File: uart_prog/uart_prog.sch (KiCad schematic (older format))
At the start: 22 parts, among them J1 USB_B_Micro, J2 Conn_01x06, Q1 MBT3904DW1, SW1 SW_SPDT, U1 FT231XQ

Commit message: Layout doner
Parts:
- removed TP1, TP2: TestPoint, TestPoint:TestPoint_THTPad_D2.0mm_Drill1.0mm, symbol Connector:TestPoint
- C3: footprint Capacitor_SMD:C_01005_0402Metric -> Capacitor_SMD:C_0805_2012Metric_Pad1.18x1.45mm_HandSolder
- J1: symbol Connector:USB_B_Micro -> uart_prog-rescue:USB_B_Micro-Connector
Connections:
- net BOOT_OPT: now also J2.2 (Pin_2); no longer J2.4 (Pin_4)
- net EN: now also J2.1 (Pin_1); no longer J2.3 (Pin_3)
- net rx: now also J2.3 (Pin_3); no longer J2.1 (Pin_1)
- net tx: now also J2.4 (Pin_4); no longer J2.2 (Pin_2)
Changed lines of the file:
@@
 $EndComp
 $Comp
-L Connector:USB_B_Micro J1
+L uart_prog-rescue:USB_B_Micro-Connector J1
 U 1 1 608888FB
 P 2700 3450
@@
 	1    0    0    -1
 $EndComp
-Text GLabel 8400 3350 0    50   Input ~ 0
+Text GLabel 8400 3550 0    50   Input ~ 0
 rx
-Text GLabel 8400 3450 0    50   Input ~ 0
+Text GLabel 8400 3650 0    50   Input ~ 0
 tx
 Text GLabel 8400 3750 0    50   Input ~ 0
 5v
-Text GLabel 8400 3550 0    50   Input ~ 0
+Text GLabel 8400 3350 0    50   Input ~ 0
 EN
-Text GLabel 8400 3650 0    50   Input ~ 0
+Text GLabel 8400 3450 0    50   Input ~ 0
 BOOT_OPT
 $Comp
@@
 F 0 "C3" H 4392 2596 50  0000 L CNN
 F 1 "22u" H 4392 2505 50  0000 L CNN
-F 2 "Capacitor_SMD:C_01005_0402Metric" H 4300 2550 50  0001 C CNN
+F 2 "Capacitor_SMD:C_0805_2012Metric_Pad1.18x1.45mm_HandSolder" H 4300 2550 50  0001 C CNN
 F 3 "~" H 4300 2550 50  0001 C CNN
 	1    4300 2550
@@
 Text GLabel 8200 2350 3    50   Input ~ 0
 rxled
+Text GLabel 8200 1950 1    50   Input ~ 0
+vccio
+$Comp
+L Device:R_Small R6
+U 1 1 6090552B
+P 8600 2050
+F 0 "R6" V 8404 2050 50  0000 C CNN
+F 1 "270" V 8495 2050 50  0000 C CNN
+F 2 "Resistor_SMD:R_0805_2012Metric_Pad1.15x1.40mm_HandSolder" H 8600 2050 50  0001 C CNN
+F 3 "~" H 8600 2050 50  0001 C CNN
+	1    8600 2050
+	-1   0    0    1
+$EndComp
+Text GLabel 8600 2350 3    50   Input ~ 0
+txled
+Text GLabel 8600 1950 1    50   Input ~ 0
+vccio
+Text Label 3300 3450 0    50   ~ 0
+in+
+Text Label 3250 3550 0    50   ~ 0
+in-
+Text Label 4300 3500 0    50   ~ 0
+in2+
+Text Label 4250 3450 0    50   ~ 0
+in2-
+$Comp
+L Device:LED_Small D2
+U 1 1 60905532
+P 8600 2250
+F 0 "D2" V 8646 2182 50  0000 R CNN
+F 1 "yellow" V 8555 2182 50  0000 R CNN
+F 2 "LED_SMD:LED_0805_2012Metric_Pad1.15x1.40mm_HandSolder" V 8600 2250 50  0001 C CNN
+F 3 "~" V 8600 2250 50  0001 C CNN
+	1    8600 2250
+	0    -1   -1   0
+$EndComp
 $Comp
 L Device:LED_Small D1
@@
 	0    -1   -1   0
 $EndComp
-Text GLabel 8200 1950 1    50   Input ~ 0
-vccio
-$Comp
-L Device:R_Small R6
-U 1 1 6090552B
-P 8600 2050
-F 0 "R6" V 8404 2050 50  0000 C CNN
-F 1 "270" V 8495 2050 50  0000 C CNN
-F 2 "Resistor_SMD:R_0805_2012Metric_Pad1.15x1.40mm_HandSolder" H 8600 2050 50  0001 C CNN
-F 3 "~" H 8600 2050 50  0001 C CNN
-	1    8600 2050
-	-1   0    0    1
-$EndComp
-Text GLabel 8600 2350 3    50   Input ~ 0
-txled
-$Comp
-L Device:LED_Small D2
-U 1 1 60905532
-P 8600 2250
-F 0 "D2" V 8646 2182 50  0000 R CNN
-F 1 "yellow" V 8555 2182 50  0000 R CNN
-F 2 "LED_SMD:LED_0805_2012Metric_Pad1.15x1.40mm_HandSolder" V 8600 2250 50  0001 C CNN
-F 3 "~" V 8600 2250 50  0001 C CNN
-	1    8600 2250
-	0    -1   -1   0
-$EndComp
-Text GLabel 8600 1950 1    50   Input ~ 0
-vccio
-Text GLabel 8400 4350 0    50   Input ~ 0
-dtr
-Text GLabel 8400 4550 0    50   Input ~ 0
-rts
-$Comp
-L Connector:TestPoint TP1
-U 1 1 6090AF77
-P 8400 4350
-F 0 "TP1" V 8354 4538 50  0000 L CNN
-F 1 "TestPoint" V 8445 4538 50  0000 L CNN
-F 2 "TestPoint:TestPoint_THTPad_D2.0mm_Drill1.0mm" H 8600 4350 50  0001 C CNN
-F 3 "~" H 8600 4350 50  0001 C CNN
-	1    8400 4350
-	0    1    1    0
-$EndComp
-$Comp
-L Connector:TestPoint TP2
-U 1 1 6090B50B
-P 8400 4550
-F 0 "TP2" V 8354 4738 50  0000 L CNN
-F 1 "TestPoint" V 8445 4738 50  0000 L CNN
-F 2 "TestPoint:TestPoint_THTPad_D2.0mm_Drill1.0mm" H 8600 4550 50  0001 C CNN
-F 3 "~" H 8600 4550 50  0001 C CNN
-	1    8400 4550
-	0    1    1    0
-$EndComp
-Text Label 3300 3450 0    50   ~ 0
-in+
-Text Label 3250 3550 0    50   ~ 0
-in-
-Text Label 4300 3500 0    50   ~ 0
-in2+
-Text Label 4250 3450 0    50   ~ 0
-in2-
 $EndSCHEMATC

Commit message: Pcb rev1
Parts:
- J1: symbol uart_prog-rescue:USB_B_Micro-Connector -> uart_prog-rescue:USB_B_Micro-Connector-uart_prog-rescue
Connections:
- net 5v: now also J2.2 (Pin_2); no longer J2.5 (Pin_5)
- net BOOT_OPT: now also J2.5 (Pin_5); no longer J2.2 (Pin_2)
- net rx: now also J2.4 (Pin_4); no longer J2.3 (Pin_3)
- net tx: now also J2.3 (Pin_3); no longer J2.4 (Pin_4)
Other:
- moved on the sheet: D1, D2, J2, R5, R6, SW1
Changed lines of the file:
@@
 $EndComp
 $Comp
-L uart_prog-rescue:USB_B_Micro-Connector J1
+L uart_prog-rescue:USB_B_Micro-Connector-uart_prog-rescue J1
 U 1 1 608888FB
 P 2700 3450
@@
 L Switch:SW_SPDT SW1
 U 1 1 6088BAF4
-P 6850 2200
-F 0 "SW1" H 6850 1875 50  0000 C CNN
-F 1 "SW_SPDT" H 6850 1966 50  0000 C CNN
-F 2 "Connector_PinHeader_2.54mm:PinHeader_1x03_P2.54mm_Vertical" H 6850 2200 50  0001 C CNN
-F 3 "~" H 6850 2200 50  0001 C CNN
-	1    6850 2200
+P 6900 2250
+F 0 "SW1" H 6900 1925 50  0000 C CNN
+F 1 "SW_SPDT" H 6900 2016 50  0000 C CNN
+F 2 "Connector_PinHeader_2.54mm:PinHeader_1x03_P2.54mm_Vertical" H 6900 2250 50  0001 C CNN
+F 3 "~" H 6900 2250 50  0001 C CNN
+	1    6900 2250
 	-1   0    0    1
 $EndComp
-Text GLabel 6650 2100 0    50   Input ~ 0
+Text GLabel 6700 2150 0    50   Input ~ 0
 5v
-Text GLabel 6650 2300 0    50   Input ~ 0
+Text GLabel 6700 2350 0    50   Input ~ 0
 3v3
 Text GLabel 3900 3250 2    50   Input ~ 0
@@
 Text GLabel 4350 3150 0    50   Input ~ 0
 3v3
-Text GLabel 7050 2200 2    50   Input ~ 0
+Text GLabel 7100 2250 2    50   Input ~ 0
 vccio
 Text GLabel 5150 2400 1    50   Input ~ 0
@@
 L Connector_Generic:Conn_01x06 J2
 U 1 1 6089F7A4
-P 8600 3550
-F 0 "J2" H 8680 3542 50  0000 L CNN
-F 1 "Conn_01x06" H 8680 3451 50  0000 L CNN
-F 2 "Connector_PinHeader_2.54mm:PinHeader_1x06_P2.54mm_Horizontal" H 8600 3550 50  0001 C CNN
-F 3 "~" H 8600 3550 50  0001 C CNN
-	1    8600 3550
-	1    0    0    -1
-$EndComp
-Text GLabel 8400 3550 0    50   Input ~ 0
+P 8600 3850
+F 0 "J2" H 8680 3842 50  0000 L CNN
+F 1 "Conn_01x06" H 8680 3751 50  0000 L CNN
+F 2 "Connector_PinHeader_2.54mm:PinHeader_1x06_P2.54mm_Horizontal" H 8600 3850 50  0001 C CNN
+F 3 "~" H 8600 3850 50  0001 C CNN
+	1    8600 3850
+	1    0    0    -1
+$EndComp
+Text GLabel 8400 3950 0    50   Input ~ 0
 rx
-Text GLabel 8400 3650 0    50   Input ~ 0
+Text GLabel 8400 3850 0    50   Input ~ 0
 tx
 Text GLabel 8400 3750 0    50   Input ~ 0
 5v
-Text GLabel 8400 3350 0    50   Input ~ 0
+Text GLabel 8400 3650 0    50   Input ~ 0
 EN
-Text GLabel 8400 3450 0    50   Input ~ 0
+Text GLabel 8400 4050 0    50   Input ~ 0
 BOOT_OPT
 $Comp
 L power:GND #PWR0105
 U 1 1 608A10F7
-P 8400 3850
-F 0 "#PWR0105" H 8400 3600 50  0001 C CNN
-F 1 "GND" H 8405 3677 50  0000 C CNN
-F 2 "" H 8400 3850 50  0001 C CNN
-F 3 "" H 8400 3850 50  0001 C CNN
-	1    8400 3850
+P 8400 4150
+F 0 "#PWR0105" H 8400 3900 50  0001 C CNN
+F 1 "GND" H 8405 3977 50  0000 C CNN
+F 2 "" H 8400 4150 50  0001 C CNN
+F 3 "" H 8400 4150 50  0001 C CNN
+	1    8400 4150
 	1    0    0    -1
 $EndComp
@@
 L Device:R_Small R5
 U 1 1 60902AA0
-P 8200 2050
-F 0 "R5" V 8004 2050 50  0000 C CNN
-F 1 "270" V 8095 2050 50  0000 C CNN
-F 2 "Resistor_SMD:R_0805_2012Metric_Pad1.15x1.40mm_HandSolder" H 8200 2050 50  0001 C CNN
-F 3 "~" H 8200 2050 50  0001 C CNN
-	1    8200 2050
+P 8200 2350
+F 0 "R5" V 8004 2350 50  0000 C CNN
+F 1 "270" V 8095 2350 50  0000 C CNN
+F 2 "Resistor_SMD:R_0805_2012Metric_Pad1.15x1.40mm_HandSolder" H 8200 2350 50  0001 C CNN
+F 3 "~" H 8200 2350 50  0001 C CNN
+	1    8200 2350
 	-1   0    0    1
 $EndComp
 Text GLabel 5750 4150 2    50   Input ~ 0
 rxled
-Text GLabel 8200 2350 3    50   Input ~ 0
+Text GLabel 8200 2650 3    50   Input ~ 0
 rxled
-Text GLabel 8200 1950 1    50   Input ~ 0
+Text GLabel 8200 2250 1    50   Input ~ 0
 vccio
 $Comp
 L Device:R_Small R6
 U 1 1 6090552B
-P 8600 2050
-F 0 "R6" V 8404 2050 50  0000 C CNN
-F 1 "270" V 8495 2050 50  0000 C CNN
-F 2 "Resistor_SMD:R_0805_2012Metric_Pad1.15x1.40mm_HandSolder" H 8600 2050 50  0001 C CNN
-F 3 "~" H 8600 2050 50  0001 C CNN
-	1    8600 2050
+P 8600 2350
+F 0 "R6" V 8404 2350 50  0000 C CNN
+F 1 "270" V 8495 2350 50  0000 C CNN
+F 2 "Resistor_SMD:R_0805_2012Metric_Pad1.15x1.40mm_HandSolder" H 8600 2350 50  0001 C CNN
+F 3 "~" H 8600 2350 50  0001 C CNN
+	1    8600 2350
 	-1   0    0    1
 $EndComp
-Text GLabel 8600 2350 3    50   Input ~ 0
+Text GLabel 8600 2650 3    50   Input ~ 0
 txled
-Text GLabel 8600 1950 1    50   Input ~ 0
+Text GLabel 8600 2250 1    50   Input ~ 0
 vccio
 Text Label 3300 3450 0    50   ~ 0
@@
 L Device:LED_Small D2
 U 1 1 60905532
-P 8600 2250
-F 0 "D2" V 8646 2182 50  0000 R CNN
-F 1 "yellow" V 8555 2182 50  0000 R CNN
-F 2 "LED_SMD:LED_0805_2012Metric_Pad1.15x1.40mm_HandSolder" V 8600 2250 50  0001 C CNN
-F 3 "~" V 8600 2250 50  0001 C CNN
-	1    8600 2250
+P 8600 2550
+F 0 "D2" V 8646 2482 50  0000 R CNN
+F 1 "yellow" V 8555 2482 50  0000 R CNN
+F 2 "LED_SMD:LED_0805_2012Metric_Pad1.15x1.40mm_HandSolder" V 8600 2550 50  0001 C CNN
+F 3 "~" V 8600 2550 50  0001 C CNN
+	1    8600 2550
 	0    -1   -1   0
 $EndComp
@@
 L Device:LED_Small D1
 U 1 1 609039AE
-P 8200 2250
-F 0 "D1" V 8246 2182 50  0000 R CNN
-F 1 "green" V 8155 2182 50  0000 R CNN
-F 2 "LED_SMD:LED_0805_2012Metric_Pad1.15x1.40mm_HandSolder" V 8200 2250 50  0001 C CNN
-F 3 "~" V 8200 2250 50  0001 C CNN
-	1    8200 2250
+P 8200 2550
+F 0 "D1" V 8246 2482 50  0000 R CNN
+F 1 "green" V 8155 2482 50  0000 R CNN
+F 2 "LED_SMD:LED_0805_2012Metric_Pad1.15x1.40mm_HandSolder" V 8200 2550 50  0001 C CNN
+F 3 "~" V 8200 2550 50  0001 C CNN
+	1    8200 2550
 	0    -1   -1   0
 $EndComp

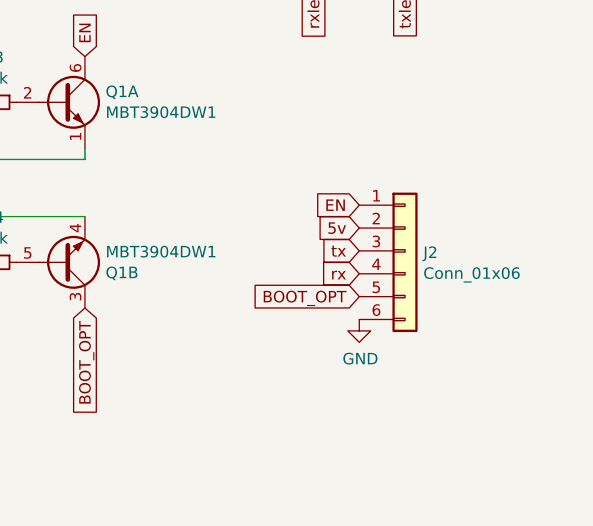
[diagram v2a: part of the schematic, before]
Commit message: Updata schema to reflect board rev2
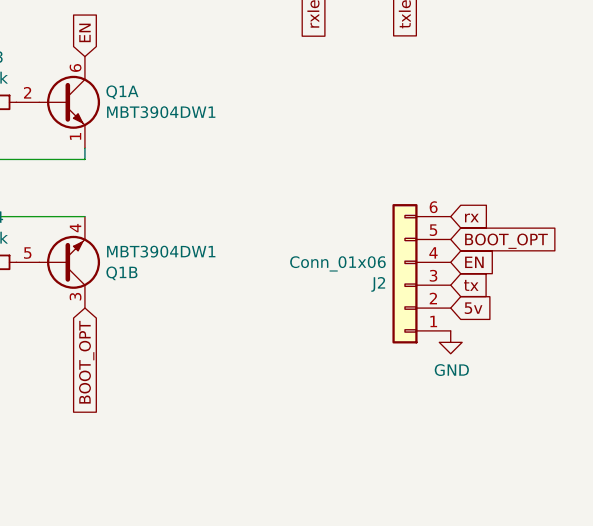
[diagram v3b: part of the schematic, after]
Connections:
- net EN: now also J2.4 (Pin_4); no longer J2.1 (Pin_1)
- net GND: now also J2.1 (Pin_1); no longer J2.6 (Pin_6)
- net rx: now also J2.6 (Pin_6); no longer J2.4 (Pin_4)
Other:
- moved on the sheet: J2
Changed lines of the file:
@@
 L Connector_Generic:Conn_01x06 J2
 U 1 1 6089F7A4
-P 8600 3850
-F 0 "J2" H 8680 3842 50  0000 L CNN
-F 1 "Conn_01x06" H 8680 3751 50  0000 L CNN
-F 2 "Connector_PinHeader_2.54mm:PinHeader_1x06_P2.54mm_Horizontal" H 8600 3850 50  0001 C CNN
-F 3 "~" H 8600 3850 50  0001 C CNN
-	1    8600 3850
-	1    0    0    -1
+P 8600 4000
+F 0 "J2" H 8680 3992 50  0000 L CNN
+F 1 "Conn_01x06" H 8680 3901 50  0000 L CNN
+F 2 "Connector_PinHeader_2.54mm:PinHeader_1x06_P2.54mm_Horizontal" H 8600 4000 50  0001 C CNN
+F 3 "~" H 8600 4000 50  0001 C CNN
+	1    8600 4000
+	-1   0    0    1
 $EndComp
-Text GLabel 8400 3950 0    50   Input ~ 0
+Text GLabel 8800 3700 2    50   Input ~ 0
 rx
-Text GLabel 8400 3850 0    50   Input ~ 0
+Text GLabel 8800 4000 2    50   Input ~ 0
 tx
-Text GLabel 8400 3750 0    50   Input ~ 0
+Text GLabel 8800 4100 2    50   Input ~ 0
 5v
-Text GLabel 8400 3650 0    50   Input ~ 0
+Text GLabel 8800 3900 2    50   Input ~ 0
 EN
-Text GLabel 8400 4050 0    50   Input ~ 0
+Text GLabel 8800 3800 2    50   Input ~ 0
 BOOT_OPT
 $Comp
 L power:GND #PWR0105
 U 1 1 608A10F7
-P 8400 4150
-F 0 "#PWR0105" H 8400 3900 50  0001 C CNN
-F 1 "GND" H 8405 3977 50  0000 C CNN
-F 2 "" H 8400 4150 50  0001 C CNN
-F 3 "" H 8400 4150 50  0001 C CNN
-	1    8400 4150
+P 8800 4200
+F 0 "#PWR0105" H 8800 3950 50  0001 C CNN
+F 1 "GND" H 8805 4027 50  0000 C CNN
+F 2 "" H 8800 4200 50  0001 C CNN
+F 3 "" H 8800 4200 50  0001 C CNN
+	1    8800 4200
 	1    0    0    -1
 $EndComp

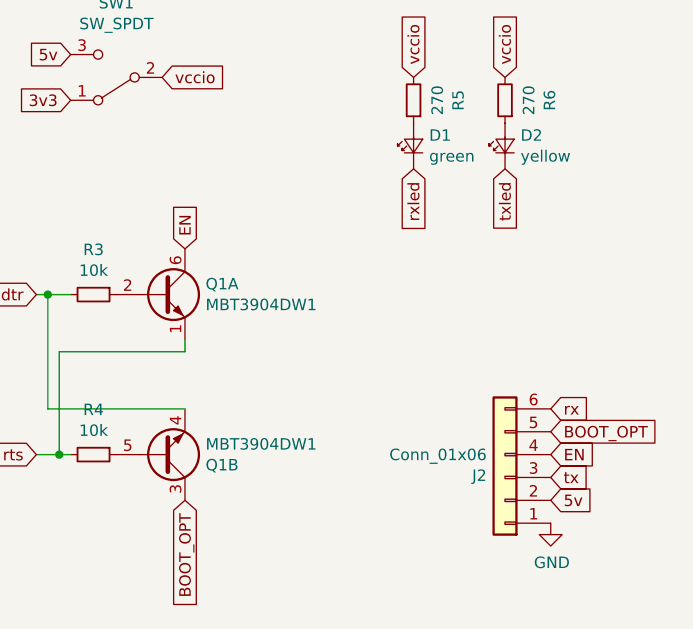
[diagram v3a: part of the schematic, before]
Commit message: rename en to reset
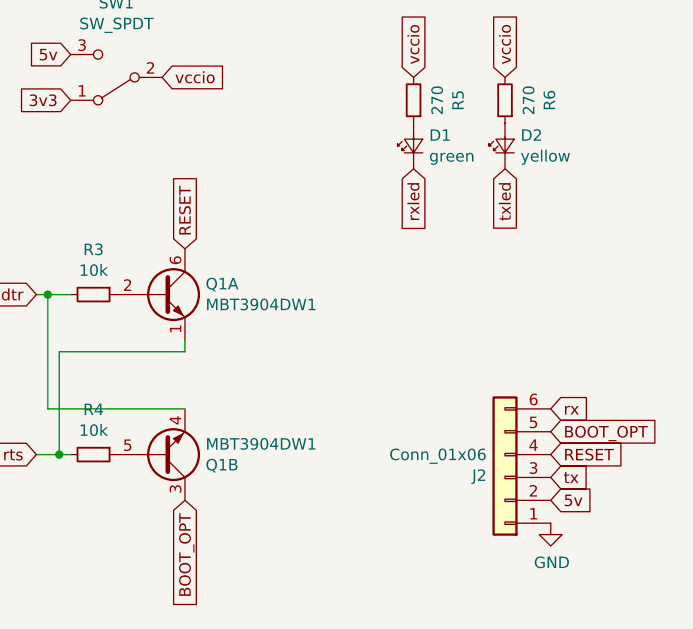
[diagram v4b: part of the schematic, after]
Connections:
- net EN renamed RESET
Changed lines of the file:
@@
 $EndComp
 Text GLabel 7200 3000 1    50   Input ~ 0
-EN
+RESET
 Text GLabel 7200 4100 3    50   Input ~ 0
 BOOT_OPT
@@
 5v
 Text GLabel 8800 3900 2    50   Input ~ 0
-EN
+RESET
 Text GLabel 8800 3800 2    50   Input ~ 0
 BOOT_OPT
